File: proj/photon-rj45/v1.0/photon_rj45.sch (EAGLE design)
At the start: 79 parts, among them J1 PJ-036AH, J2 PJ-036AH, J3 54602-908LF, J5 54602-908LF, U1 PHOTONH, U2 PCA9615DPJ, U3 MIC4680YM-TR, U4 LM2937IMP3.3NOPB

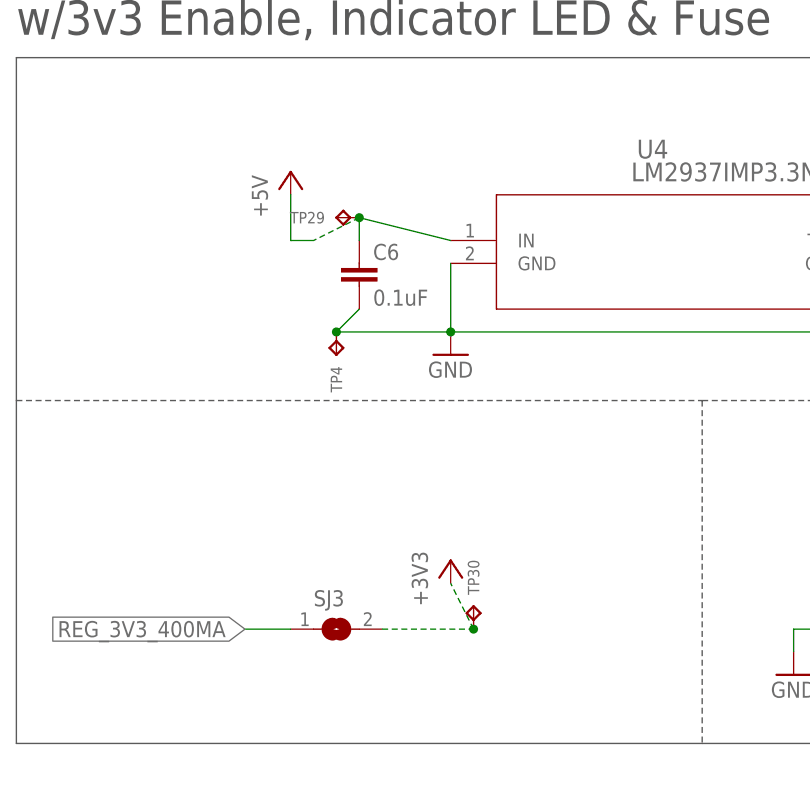
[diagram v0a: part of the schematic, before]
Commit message: added atlas sensor port design block
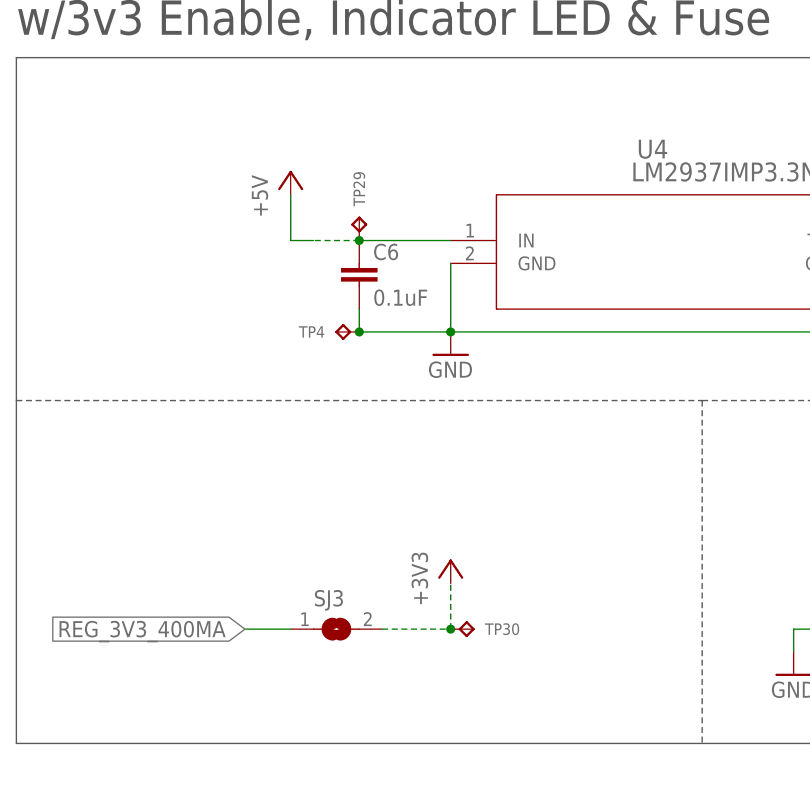
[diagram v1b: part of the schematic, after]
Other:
- moved on the sheet: TP29, TP30, TP4
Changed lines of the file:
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@@
 <instance part="F2" gate="A" x="-40.64" y="-22.86"/>
 <instance part="+3V3" gate="G$1" x="-104.14" y="-55.88"/>
-<instance part="TP4" gate="G$1" x="-116.84" y="-30.48" rot="R90"/>
-<instance part="TP29" gate="G$1" x="-114.3" y="-17.78"/>
-<instance part="TP30" gate="G$1" x="-101.6" y="-63.5" rot="R270"/>
+<instance part="TP4" gate="G$1" x="-114.3" y="-30.48"/>
+<instance part="TP29" gate="G$1" x="-114.3" y="-20.32" rot="R270"/>
+<instance part="TP30" gate="G$1" x="-104.14" y="-63.5" rot="R180"/>
 <instance part="P+1" gate="1" x="-121.92" y="-12.7"/>
 <instance part="C4" gate="G$1" x="43.18" y="-50.8"/>
@@
 <pinref part="C6" gate="G$1" pin="2"/>
 <pinref part="GND12" gate="1" pin="GND"/>
-<wire x1="-114.3" y1="-27.94" x2="-116.84" y2="-30.48" width="0.1524" layer="91"/>
-<wire x1="-116.84" y1="-30.48" x2="-104.14" y2="-30.48" width="0.1524" layer="91"/>
+<wire x1="-114.3" y1="-27.94" x2="-114.3" y2="-30.48" width="0.1524" layer="91"/>
+<wire x1="-114.3" y1="-30.48" x2="-104.14" y2="-30.48" width="0.1524" layer="91"/>
 <pinref part="U4" gate="A" pin="GND"/>
 <wire x1="-104.14" y1="-30.48" x2="-104.14" y2="-22.86" width="0.1524" layer="91"/>
@@
 <wire x1="-104.14" y1="-30.48" x2="-50.8" y2="-30.48" width="0.1524" layer="91"/>
 <pinref part="TP4" gate="G$1" pin="TP"/>
-<junction x="-116.84" y="-30.48"/>
+<junction x="-114.3" y="-30.48"/>
 </segment>
 <segment>
@@
 <pinref part="SJ3" gate="1" pin="2"/>
 <pinref part="+3V3" gate="G$1" pin="+3V3"/>
-<wire x1="-111.76" y1="-63.5" x2="-101.6" y2="-63.5" width="0.1524" layer="91" style="longdash"/>
-<wire x1="-101.6" y1="-63.5" x2="-104.14" y2="-58.42" width="0.1524" layer="91" style="longdash"/>
+<wire x1="-111.76" y1="-63.5" x2="-104.14" y2="-63.5" width="0.1524" layer="91" style="longdash"/>
+<wire x1="-104.14" y1="-63.5" x2="-104.14" y2="-58.42" width="0.1524" layer="91" style="longdash"/>
 <pinref part="TP30" gate="G$1" pin="TP"/>
-<junction x="-101.6" y="-63.5"/>
+<junction x="-104.14" y="-63.5"/>
 </segment>
 <segment>
@@
 <pinref part="U4" gate="A" pin="IN"/>
 <pinref part="C6" gate="G$1" pin="1"/>
-<wire x1="-104.14" y1="-20.32" x2="-114.3" y2="-17.78" width="0.1524" layer="91"/>
-<junction x="-114.3" y="-17.78"/>
-<wire x1="-114.3" y1="-17.78" x2="-119.38" y2="-20.32" width="0.1524" layer="91" style="longdash"/>
+<wire x1="-104.14" y1="-20.32" x2="-114.3" y2="-20.32" width="0.1524" layer="91"/>
+<junction x="-114.3" y="-20.32"/>
+<wire x1="-114.3" y1="-20.32" x2="-119.38" y2="-20.32" width="0.1524" layer="91" style="longdash"/>
 <pinref part="TP29" gate="G$1" pin="TP"/>
 <pinref part="P+1" gate="1" pin="+5V"/>
 <wire x1="-119.38" y1="-20.32" x2="-121.92" y2="-20.32" width="0.1524" layer="91"/>
 <wire x1="-121.92" y1="-20.32" x2="-121.92" y2="-15.24" width="0.1524" layer="91"/>
-<wire x1="-114.3" y1="-20.32" x2="-114.3" y2="-17.78" width="0.1524" layer="91"/>
-</segment>
-<segment>
+</segment>
+<segment>
